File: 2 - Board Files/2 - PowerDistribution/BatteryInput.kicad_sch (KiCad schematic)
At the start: 0 parts

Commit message: Added sch and pcb for initial power input stage
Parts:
- added C201, C202, C203, C204, C205: 10u, Capacitor_SMD:CP_Elec_6.3x5.4, symbol Device:C_Small
- added C206, C208, C210, C212, C214, C216: 10n, Capacitor_SMD:C_0402_1005Metric, symbol Device:C_Small
- added C207, C209, C211, C213, C215, C217: 1u, Capacitor_SMD:C_0603_1608Metric, symbol Device:C_Small
- added C218: 100n, Capacitor_SMD:C_0402_1005Metric, symbol Device:C_Small
- added D201, D202: D, Diode_SMD:D_SMB, symbol Device:D
- added D203, D204, D205: LED, LED_SMD:LED_0603_1608Metric, symbol Device:LED
- added D? (x2): D_TVS, symbol Device:D_TVS
- added F201: Polyfuse, Resistor_THT:R_Axial_DIN0309_L9.0mm_D3.2mm_P2.54mm_Vertical, symbol Device:Polyfuse
- added J201: Battery Input, Connector_AMASS:AMASS_XT60-F_1x02_P7.20mm_Vertical, symbol Connector:Conn_01x02_Male
- added J202: Battery Balance Connector, Connector_JST:JST_EH_S4B-EH_1x04_P2.50mm_Horizontal, symbol Connector:Conn_01x04_Male
- added R201: BATT_SNS_SHUNT, Resistor_SMD:R_1206_3216Metric, symbol Device:R_Small_US
- added R202: CTL_PWR_SHUNT, Resistor_SMD:R_1206_3216Metric, symbol Device:R_Small_US
- added R203, R204, R205, R206, R207, R208, R209, R210, R211, R212, R213: R_Small_US, Resistor_SMD:R_0402_1005Metric, symbol Device:R_Small_US
- added U201, U202: MAX40056F, Package_SO:MSOP-8_3x3mm_P0.65mm, symbol QuadrotorLib:MAX40056F
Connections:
- new net: D204.2 (A), R212.1
- new net: C214.1, C215.1, R207.1, U201.5 (REF)
- new net: R205.1, U201.4 (OUT)
- new net: D205.2 (A), R213.1
- new net: D204.1 (K), U202.2 (COP)
- new net: R206.1, U202.4 (OUT)
- new net: C216.1, C217.1, R209.1, U202.5 (REF)
- new net: R209.2, R210.1, U202.7 (CIP)
- new net: D203.1 (K), U201.2 (COP)
- new net: D203.2 (A), R211.1
- new net: R207.2, R208.1, U201.7 (CIP)
- new net +3V3: C210.1, C211.1, C212.1, C213.1, R211.2, R212.2, U201.3 (VDD), U202.3 (VDD)
- new net +BATT: C202.1, D201.2 (A), D202.1 (K), F201.2, R203.2
- new net BAT+_IN: J201.1 (Pin_1), R201.1, R213.2, U201.1 (RS+)
- new net BAT+_IN_SNS: C201.1, F201.1, R201.2, U201.8 (RS-)
- new net BATT_CELL1: J202.2 (Pin_2)
- new net BATT_CELL2: J202.3 (Pin_3)
- new net BATT_CELL3: J202.4 (Pin_4)
- new net BATT_CURR_MON: C206.1, C207.1, R205.2
- new net BATT_V_SNS: C218.1, R203.1, R204.2
- new net GND: C201.2, C202.2, C203.2, C204.2, C205.2, C206.2, C207.2, C208.2, C209.2, C210.2, C211.2, C212.2, C213.2, C214.2, C215.2, C216.2, C217.2, C218.2, D202.2 (A), D205.1 (K), D?.1 (A1), D?.1 (A1), J201.2 (Pin_2), J202.1 (Pin_1), R204.1, R208.2, R210.2, U201.6 (GND), U202.6 (GND)
- new net VDC: C203.1, C204.1, C205.1, D?.2 (A2), D?.2 (A2), R202.2, U202.8 (RS-)
- new net VDC_CURR_MON: C208.1, C209.1, R206.2
- new net VDC_SNS_IN: D201.1 (K), R202.1, U202.1 (RS+)
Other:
- note added: "+BATT to motors"
- note added: "Get most medium gain chip"
- note added: "Input 3S Lithium Polymer battery"
- note added: "OVC FAULT"
- note added: "OVC THRESH"
- note added: "Power indication LED"
- note added: "Probably need the largest gain chip we can get"
- note added: "Rate shunt for 30A continuous"
- note added: "Rate shunt for 3A continuous"
- note added: "Rate to measure 10A forward, 1A reverse"
- note added: "Rate to measure 50A forward, 10A reverse"
- note added: "Transient suppression diodes"
- note added: "VDC to control power"
- company: (none) -> Periscope Robotics
- title: (none) -> Battery Input Connections

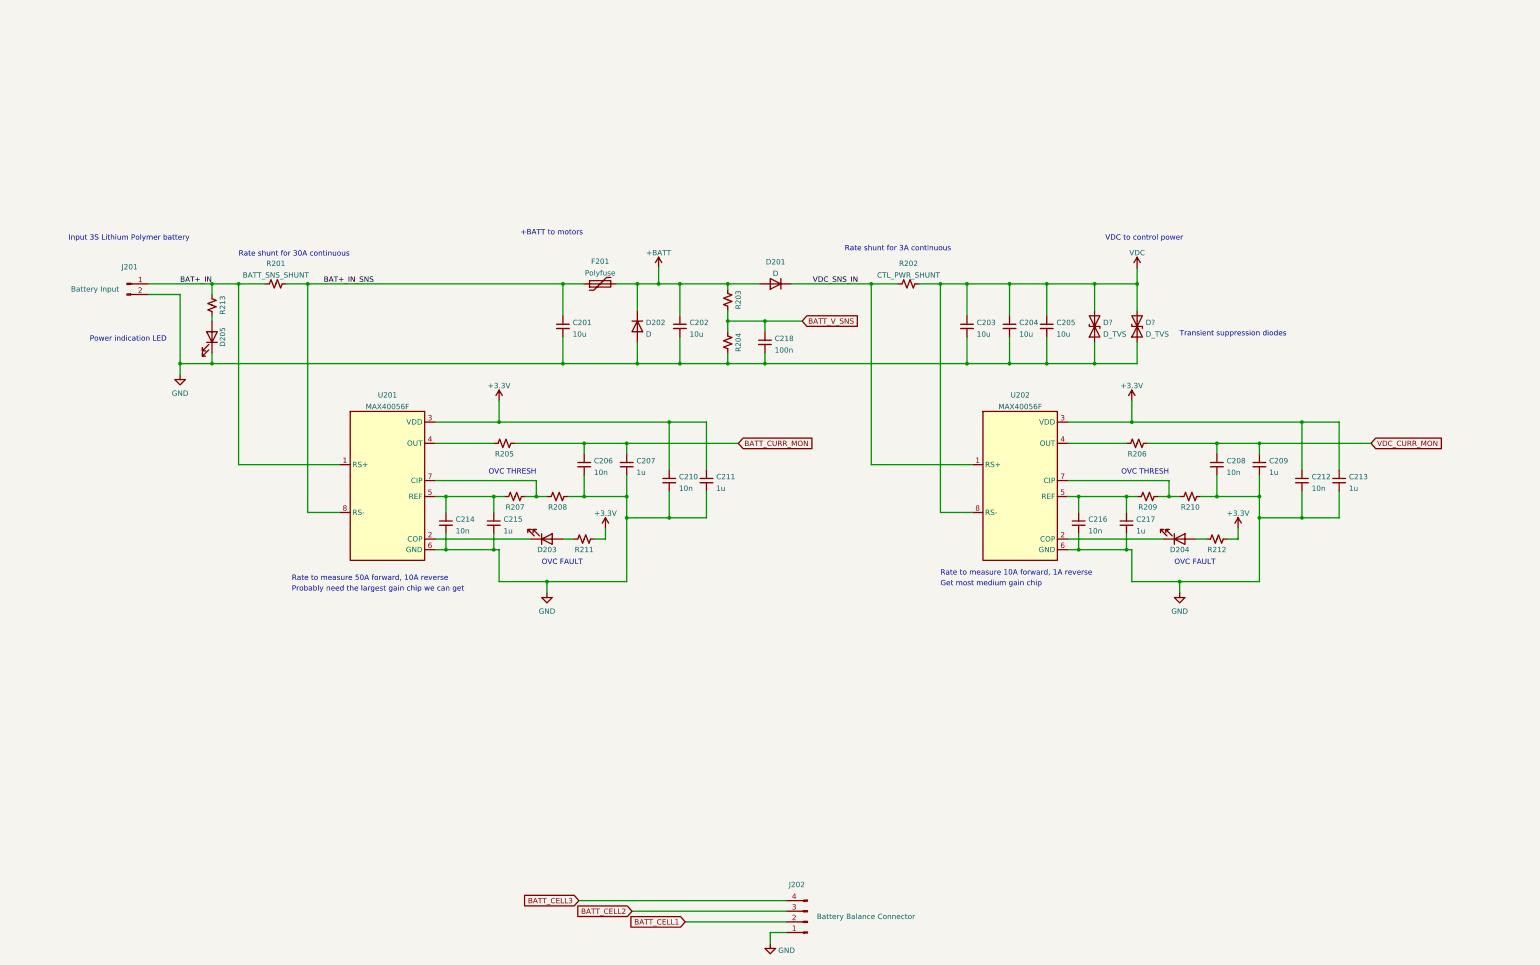
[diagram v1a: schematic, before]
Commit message: Part values for power input stage
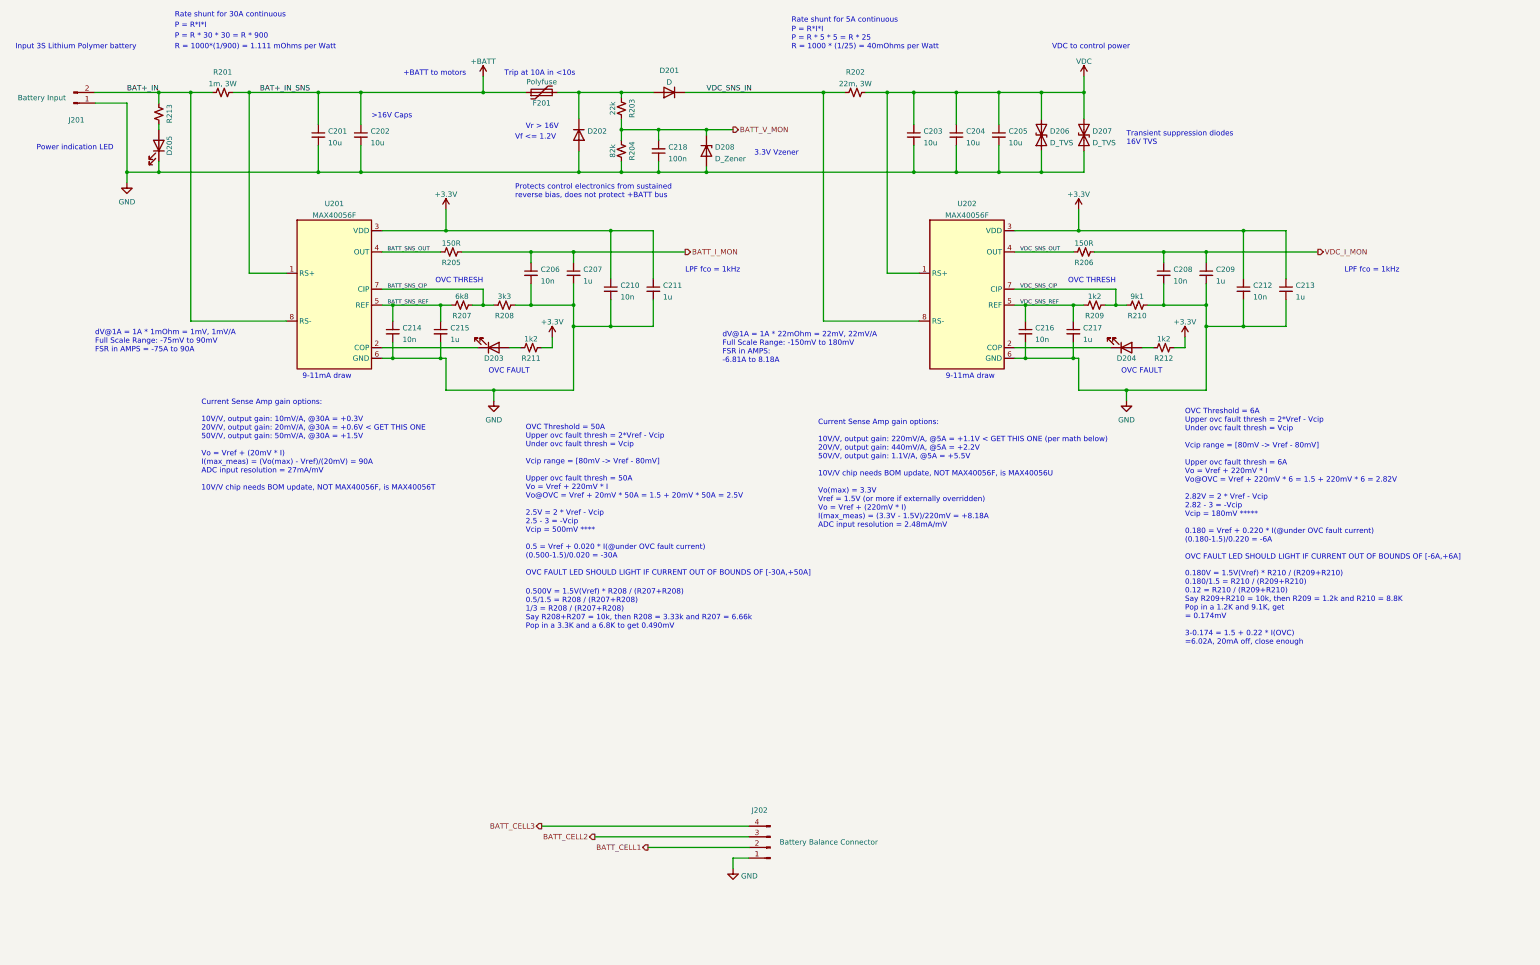
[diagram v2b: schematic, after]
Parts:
- added D208: D_Zener, Diode_SMD:D_SOD-323, symbol Device:D_Zener
- D206, D207: renamed from D?; footprint (none) -> Diode_SMD:D_SMC; PN (none) -> SMDJ10CA
- F201: footprint Resistor_THT:R_Axial_DIN0309_L9.0mm_D3.2mm_P2.54mm_Vertical -> Fuse:Fuse_2920_7451Metric; PN (none) -> 2920L500/16MR-A; Package (none) -> 2920 (7351 Metric), Concave
- R201: value BATT_SNS_SHUNT -> 1m, 3W; Part Number (none) -> CSSK3637FT1L00; Tolerance (none) -> 1%
- R202: value CTL_PWR_SHUNT -> 22m, 3W; Part Number (none) -> CSM2512FT22L0
- R203: value R_Small_US -> 22k
- R204: value R_Small_US -> 82k
- R205, R206: value R_Small_US -> 150R
- R207: value R_Small_US -> 6k8
- R208: value R_Small_US -> 3k3
- R209, R211, R212: value R_Small_US -> 1k2
- R210: value R_Small_US -> 9k1
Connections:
- net +BATT: now also C201.1, F201.1, R201.2, U201.1 (RS+); no longer D201.2 (A), D202.1 (K), F201.2, R203.2
- net BAT+_IN: now also J201.2 (Pin_2), U201.8 (RS-); no longer J201.1 (Pin_1), U201.1 (RS+)
- net GND: now also J201.1 (Pin_1), D208.2 (A); no longer J201.2 (Pin_2)
- net VDC: now also U202.1 (RS+); no longer U202.8 (RS-)
- net VDC_SNS_IN: now also U202.8 (RS-); no longer U202.1 (RS+)
- net BATT_SNS_REF: now reaches C214.1, C215.1, R207.1, U201.5 (REF)
- net BATT_SNS_OUT: now reaches R205.1, U201.4 (OUT)
- net VDC_SNS_OUT: now reaches R206.1, U202.4 (OUT)
- net VDC_SNS_REF: now reaches C216.1, C217.1, R209.1, U202.5 (REF)
- net VDC_SNS_CIP: now reaches R209.2, R210.1, U202.7 (CIP)
- net BATT_SNS_CIP: now reaches R207.2, R208.1, U201.7 (CIP)
- removed net BAT+_IN_SNS: C201.1, F201.1, R201.2, U201.8 (RS-)
- net BATT_CURR_MON renamed BATT_I_MON
- net BATT_V_SNS renamed BATT_V_MON
- net BATT_V_MON: now also D208.1 (K)
- net VDC_CURR_MON renamed VDC_I_MON
- new net: D201.2 (A), D202.1 (K), F201.2, R203.2
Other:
- note added: "0.180V = 1.5V(Vref) * R210 / (R209+R210) 0.180/1.5 = R210 / (R209+R210) 0.12 = R210 / (R209+R210) Say R209+R210 = 10k, then R209 = 1.2k and R210 = 8.8K Pop in a 1.2K and 9.1K, get = 0.174mV 3-0.174 = 1.5 + 0.22 * I(OVC) =6.02A, 20mA off, close enough"
- note added: "0.500V = 1.5V(Vref) * R208 / (R207+R208) 0.5/1.5 = R208 / (R207+R208) 1/3 = R208 / (R207+R208) Say R208+R207 = 10k, then R208 = 3.33k and R207 = 6.66k Pop in a 3.3K and a 6.8K to get 0.490mV"
- note added: "3.3V Vzener"
- note added: "9-11mA draw"
- note added: ">16V Caps"
- note added: "Current Sense Amp gain options: 10V/V, output gain: 10mV/A, @30A = +0.3V 20V/V, output gain: 20mV/A, @30A = +0.6V < GET THIS ONE 50V/V, output gain: 50mV/A, @30A = +1.5V Vo = Vref + (20mV * I) I(max_meas) = (Vo(max) - Vref)/(20mV) = 90A ADC input resolution = 27mA/mV 10V/V chip needs BOM update, NOT MAX40056F, is MAX40056T"
- note added: "Current Sense Amp gain options: 10V/V, output gain: 220mV/A, @5A = +1.1V < GET THIS ONE (per math below) 20V/V, output gain: 440mV/A, @5A = +2.2V 50V/V, output gain: 1.1V/A, @5A = +5.5V 10V/V chip needs BOM update, NOT MAX40056F, is MAX40056U Vo(max) = 3.3V Vref = 1.5V (or more if externally overridden) Vo = Vref + (220mV * I) I(max_meas) = (3.3V - 1.5V)/220mV = +8.18A ADC input resolution = 2.48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"
- note added: "LPF fco = 1kHz"
- note added: "OVC Threshold = 50A Upper ovc fault thresh = 2*Vref - Vcip Under ovc fault thresh = Vcip Vcip range = [80mV -> Vref - 80mV] Upper ovc fault thresh = 50A Vo = Vref + 220mV * I Vo@OVC = Vref + 20mV * 50A = 1.5 + 20mV * 50A = 2.5V 2.5V = 2 * Vref - Vcip 2.5 - 3 = -Vcip Vcip = 500mV **** 0.5 = Vref + 0.020 * I(@under OVC fault current) (0.500-1.5)/0.020 = -30A OVC FAULT LED SHOULD LIGHT IF CURRENT OU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"
- note added: "OVC Threshold = 6A Upper ovc fault thresh = 2*Vref - Vcip Under ovc fault thresh = Vcip Vcip range = [80mV -> Vref - 80mV] Upper ovc fault thresh = 6A Vo = Vref + 220mV * I Vo@OVC = Vref + 220mV * 6 = 1.5 + 220mV * 6 = 2.82V 2.82V = 2 * Vref - Vcip 2.82 - 3 = -Vcip Vcip = 180mV ***** 0.180 = Vref + 0.220 * I(@under OVC fault current) (0.180-1.5)/0.220 = -6A OVC FAULT LED SHOULD LIGHT IF CURRENT O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"
- note added: "P = R * 30 * 30 = R * 900"
- note added: "P = R*I*I"
- note added: "P = R*I*I P = R * 5 * 5 = R * 25 R = 1000 * (1/25) = 40mOhms per Watt"
- note added: "Protects control electronics from sustained reverse bias, does not protect +BATT bus"
- note added: "R = 1000*(1/900) = 1.111 mOhms per Watt"
- note added: "Rate shunt for 5A continuous"
- note added: "Transient suppression diodes 16V TVS"
- note added: "Trip at 10A in <10s"
- note added: "Vf <= 1.2V"
- note added: "Vr > 16V"
- note added: "dV@1A = 1A * 1mOhm = 1mV, 1mV/A Full Scale Range: -75mV to 90mV FSR in AMPS = -75A to 90A"
- note added: "dV@1A = 1A * 22mOhm = 22mV, 22mV/A Full Scale Range: -150mV to 180mV FSR in AMPS: -6.81A to 8.18A"
- note removed: "Get most medium gain chip"
- note removed: "Probably need the largest gain chip we can get"
- note removed: "Rate shunt for 3A continuous"
- note removed: "Rate to measure 10A forward, 1A reverse"
- note removed: "Rate to measure 50A forward, 10A reverse"
- note removed: "Transient suppression diodes"
- moved on the sheet: C201, C202, C203, C204, C205, C206, C207, C208, C209, C210, C211, C212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

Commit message: Added switching regulator
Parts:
- renumbered C214 to C203, C215 to C204, C206 to C205, C207 to C206, C210 to C207, C211 to C208, C218 to C209, C203 to C210, C204 to C211, C205 to C212, C216 to C213, C217 to C214, C208 to C215, C209 to C216, C212 to C217, C213 to C218, D205 to D201, D203 to D202, D202 to D203, D201 to D204, D208 to D205, D204 to D208, R213 to R201, R201 to R202, R205 to R203, R207 to R204, R208 to R205, R211 to R206, R203 to R207, R204 to R208, R202 to R209, R206 to R210, R209 to R211, R210 to R212, R212 to R213

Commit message: Motor drive initial work
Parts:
- added C219: 47u, Capacitor_SMD:CP_Elec_6.3x5.4, symbol Device:C_Small
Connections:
- net +BATT: now also C219.1
- net GND: now also C219.2
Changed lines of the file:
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@@
   (junction (at 173.99 44.45) (diameter 0) (color 0 0 0 0)
   )
+  (junction (at 139.7 44.45) (diameter 0) (color 0 0 0 0)
+  )
   (junction (at 172.72 100.33) (diameter 0) (color 0 0 0 0)
   )
   (junction (at 153.67 115.57) (diameter 0) (color 0 0 0 0)
   )
+  (junction (at 139.7 63.5) (diameter 0) (color 0 0 0 0)
+  )
   (junction (at 111.76 63.5) (diameter 0) (color 0 0 0 0)
   )
@@
     (stroke (width 0) (type default) (color 0 0 0 0))
   )
+  (wire (pts (xy 139.7 63.5) (xy 173.99 63.5))
+    (stroke (width 0) (type default) (color 0 0 0 0))
+  )
   (wire (pts (xy 129.54 104.14) (xy 129.54 107.95))
     (stroke (width 0) (type default) (color 0 0 0 0))
@@
     (stroke (width 0) (type default) (color 0 0 0 0))
   )
+  (wire (pts (xy 139.7 57.15) (xy 139.7 63.5))
+    (stroke (width 0) (type default) (color 0 0 0 0))
+  )
   (wire (pts (xy 129.54 95.25) (xy 140.97 95.25))
     (stroke (width 0) (type default) (color 0 0 0 0))
@@
     (stroke (width 0) (type default) (color 0 0 0 0))
   )
-  (wire (pts (xy 121.92 44.45) (xy 151.13 44.45))
+  (wire (pts (xy 121.92 44.45) (xy 139.7 44.45))
     (stroke (width 0) (type default) (color 0 0 0 0))
   )
@@
     (stroke (width 0) (type default) (color 0 0 0 0))
   )
-  (wire (pts (xy 121.92 63.5) (xy 173.99 63.5))
+  (wire (pts (xy 121.92 63.5) (xy 139.7 63.5))
     (stroke (width 0) (type default) (color 0 0 0 0))
   )
@@
     (stroke (width 0) (type default) (color 0 0 0 0))
   )
+  (wire (pts (xy 139.7 44.45) (xy 151.13 44.45))
+    (stroke (width 0) (type default) (color 0 0 0 0))
+  )
   (wire (pts (xy 323.85 82.55) (xy 350.52 82.55))
     (stroke (width 0) (type default) (color 0 0 0 0))
@@
   )
   (wire (pts (xy 280.67 104.14) (xy 280.67 107.95))
+    (stroke (width 0) (type default) (color 0 0 0 0))
+  )
+  (wire (pts (xy 139.7 44.45) (xy 139.7 52.07))
     (stroke (width 0) (type default) (color 0 0 0 0))
   )
@@
     (pin "4")
   )
+  (symbol (lib_id "Device:C_Small") (at 139.7 54.61 0) (mirror y) (unit 1)
+    (in_bom yes) (on_board yes) (fields_autoplaced)
+    (property "Reference" "C219" (id 0) (at 142.0241 53.7078 0)
+      (effects (font (size 1.27 1.27)) (justify right))
+    )
+    (property "Value" "47u" (id 1) (at 142.0241 56.4829 0)
+      (effects (font (size 1.27 1.27)) (justify right))
+    )
+    (property "Footprint" "Capacitor_SMD:CP_Elec_6.3x5.4" (id 2) (at 139.7 54.61 0)
+      (effects (font (size 1.27 1.27)) hide)
+    )
+    (property "Datasheet" "~" (id 3) (at 139.7 54.61 0)
+      (effects (font (size 1.27 1.27)) hide)
+    )
+    (pin "1")
+    (pin "2")
+  )
   (symbol (lib_id "Device:LED") (at 304.8 105.41 0) (mirror x) (unit 1)

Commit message: MOSFETs changed
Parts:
- F201: footprint Fuse:Fuse_2920_7451Metric -> QuadrotorFootprints:Fuse_2920_7451Metric
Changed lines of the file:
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@@
     (property "Reference" "F201" (id 0) (at 165.1 46.99 90))
     (property "Value" "Polyfuse" (id 1) (at 165.1 41.91 90))
-    (property "Footprint" "Fuse:Fuse_2920_7451Metric" (id 2) (at 170.18 43.18 0)
+    (property "Footprint" "QuadrotorFootprints:Fuse_2920_7451Metric" (id 2) (at 170.18 43.18 0)
       (effects (font (size 1.27 1.27)) (justify left) hide)
     )
